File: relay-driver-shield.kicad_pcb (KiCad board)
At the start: 2 copper layers, 21 parts, among them J1 Screw_Terminal_01x02, J2 Screw_Terminal_01x02, J3 Screw_Terminal_01x02, J4 Screw_Terminal_01x02, Q1 2N7002, Q2 2N7002, Q3 2N7002, Q4 2N7002

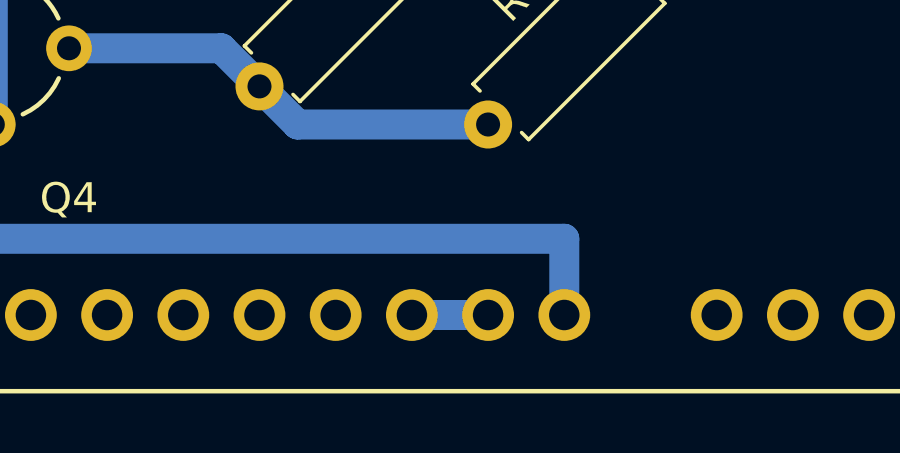
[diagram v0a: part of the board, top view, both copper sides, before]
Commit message: Removed bridge between GND1, GND2 and GND3 Not needed and avoids problems with Electrical Rule Checker
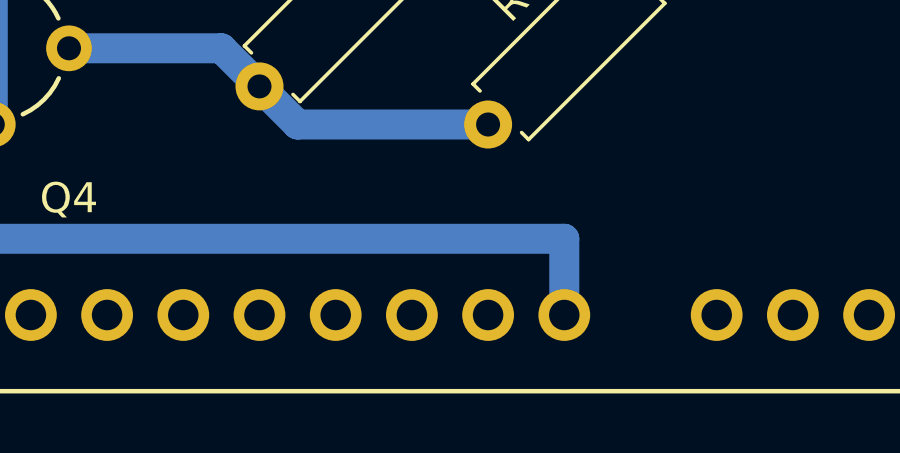
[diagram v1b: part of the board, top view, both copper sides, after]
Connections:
- ARD1 pad GND2: GND -> (no net)
- ARD1 pad GND3: GND -> (no net)
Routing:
- net GND: track 104.6 -> 102.0 mm
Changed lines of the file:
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@@
 (kicad_pcb (version 4) (host pcbnew 4.0.7)
   (general
-    (links 38)
-    (no_connects 1)
-    (area 102.594999 58.969 178.075001 114.75)
+    (links 36)
+    (no_connects 0)
+    (area 0 0 0 0)
     (thickness 1.6)
     (drawings 0)
-    (tracks 95)
+    (tracks 94)
     (zones 0)
     (modules 21)
@@
     (pad VIN thru_hole oval (at 45.72 -2.54) (size 1.7272 1.7272) (drill 1.016) (layers *.Cu *.Mask)
       (net 1 +12V))
-    (pad GND3 thru_hole oval (at 43.18 -2.54) (size 1.7272 1.7272) (drill 1.016) (layers *.Cu *.Mask)
-      (net 2 GND))
-    (pad GND2 thru_hole oval (at 40.64 -2.54) (size 1.7272 1.7272) (drill 1.016) (layers *.Cu *.Mask)
-      (net 2 GND))
+    (pad GND3 thru_hole oval (at 43.18 -2.54) (size 1.7272 1.7272) (drill 1.016) (layers *.Cu *.Mask))
+    (pad GND2 thru_hole oval (at 40.64 -2.54) (size 1.7272 1.7272) (drill 1.016) (layers *.Cu *.Mask))
     (pad 5V1 thru_hole oval (at 38.1 -2.54) (size 1.7272 1.7272) (drill 1.016) (layers *.Cu *.Mask))
     (pad 3.3V thru_hole oval (at 35.56 -2.54) (size 1.7272 1.7272) (drill 1.016) (layers *.Cu *.Mask))
@@
   (segment (start 129.54 100.33) (end 115.57 100.33) (width 1) (layer B.Cu) (net 1))
   (segment (start 129.54 90.17) (end 115.57 90.17) (width 1) (layer B.Cu) (net 1))
-  (segment (start 150.168154 68.271846) (end 135.636 68.271846) (width 1) (layer B.Cu) (net 2) (status 400000))
+  (segment (start 150.168154 68.271846) (end 135.636 68.271846) (width 1) (layer B.Cu) (net 2))
   (segment (start 135.89 68.58) (end 135.636 68.58) (width 1) (layer B.Cu) (net 2))
   (segment (start 135.89 68.525846) (end 135.89 68.58) (width 1) (layer B.Cu) (net 2))
   (segment (start 135.636 68.271846) (end 135.89 68.525846) (width 1) (layer B.Cu) (net 2))
-  (segment (start 150.168154 98.751846) (end 135.89 98.751846) (width 1) (layer B.Cu) (net 2) (status 400000))
+  (segment (start 150.168154 98.751846) (end 135.89 98.751846) (width 1) (layer B.Cu) (net 2))
   (segment (start 135.89 98.751846) (end 135.89 99.06) (width 1) (layer B.Cu) (net 2))
-  (segment (start 150.168154 88.591846) (end 135.89 88.591846) (width 1) (layer B.Cu) (net 2) (status 400000))
+  (segment (start 150.168154 88.591846) (end 135.89 88.591846) (width 1) (layer B.Cu) (net 2))
   (segment (start 135.89 88.591846) (end 135.89 88.9) (width 1) (layer B.Cu) (net 2))
-  (segment (start 150.168154 78.431846) (end 135.89 78.431846) (width 1) (layer B.Cu) (net 2) (status 400000))
+  (segment (start 150.168154 78.431846) (end 135.89 78.431846) (width 1) (layer B.Cu) (net 2))
   (segment (start 135.89 78.431846) (end 135.89 78.74) (width 1) (layer B.Cu) (net 2))
-  (segment (start 135.89 95.25) (end 135.89 99.06) (width 1) (layer B.Cu) (net 2) (status 400000))
-  (segment (start 135.89 99.06) (end 135.89 105.41) (width 1) (layer B.Cu) (net 2) (status 800000))
-  (segment (start 135.89 85.09) (end 135.89 88.9) (width 1) (layer B.Cu) (net 2) (status 400000))
-  (segment (start 135.89 88.9) (end 135.89 95.25) (width 1) (layer B.Cu) (net 2) (status 800000))
-  (segment (start 135.89 74.93) (end 135.89 78.74) (width 1) (layer B.Cu) (net 2) (status 400000))
-  (segment (start 135.89 78.74) (end 135.89 85.09) (width 1) (layer B.Cu) (net 2) (status 800000))
-  (segment (start 135.636 63.5) (end 135.636 68.58) (width 1) (layer B.Cu) (net 2) (status 400000))
-  (segment (start 135.636 68.58) (end 135.636 74.676) (width 1) (layer B.Cu) (net 2) (status 800000))
-  (segment (start 135.636 74.676) (end 135.89 74.93) (width 1) (layer B.Cu) (net 2) (status C00000))
-  (segment (start 149.86 111.76) (end 152.4 111.76) (width 1) (layer B.Cu) (net 2))
+  (segment (start 135.89 95.25) (end 135.89 99.06) (width 1) (layer B.Cu) (net 2))
+  (segment (start 135.89 99.06) (end 135.89 105.41) (width 1) (layer B.Cu) (net 2))
+  (segment (start 135.89 85.09) (end 135.89 88.9) (width 1) (layer B.Cu) (net 2))
+  (segment (start 135.89 88.9) (end 135.89 95.25) (width 1) (layer B.Cu) (net 2))
+  (segment (start 135.89 74.93) (end 135.89 78.74) (width 1) (layer B.Cu) (net 2))
+  (segment (start 135.89 78.74) (end 135.89 85.09) (width 1) (layer B.Cu) (net 2))
+  (segment (start 135.636 63.5) (end 135.636 68.58) (width 1) (layer B.Cu) (net 2))
+  (segment (start 135.636 68.58) (end 135.636 74.676) (width 1) (layer B.Cu) (net 2))
+  (segment (start 135.636 74.676) (end 135.89 74.93) (width 1) (layer B.Cu) (net 2))
   (segment (start 150.476308 78.74) (end 150.168154 78.431846) (width 0.25) (layer B.Cu) (net 2) (status 30))
   (segment (start 150.168154 68.271846) (end 149.551846 68.271846) (width 0.25) (layer B.Cu) (net 2) (status 30))

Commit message: Added values to the resistors and diodes
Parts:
- D1, D2, D3, D4: value D -> 1N4004
- R1, R3, R5, R7: value R -> 1K
- R2, R4, R6, R8: value R -> 10K
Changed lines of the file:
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@@
       (effects (font (size 1 1) (thickness 0.15)))
     )
-    (fp_text value D (at 3.81 2.41 225) (layer F.Fab)
+    (fp_text value 1N4004 (at 3.81 2.41 225) (layer F.Fab)
       (effects (font (size 1 1) (thickness 0.15)))
     )
@@
       (effects (font (size 1 1) (thickness 0.15)))
     )
-    (fp_text value D (at 3.81 2.41 225) (layer F.Fab)
+    (fp_text value 1N4004 (at 3.81 2.41 225) (layer F.Fab)
       (effects (font (size 1 1) (thickness 0.15)))
     )
@@
       (effects (font (size 1 1) (thickness 0.15)))
     )
-    (fp_text value D (at 3.81 2.41 225) (layer F.Fab)
+    (fp_text value 1N4004 (at 3.81 2.41 225) (layer F.Fab)
       (effects (font (size 1 1) (thickness 0.15)))
     )
@@
       (effects (font (size 1 1) (thickness 0.15)))
     )
-    (fp_text value D (at 3.81 2.41 225) (layer F.Fab)
+    (fp_text value 1N4004 (at 3.81 2.41 225) (layer F.Fab)
       (effects (font (size 1 1) (thickness 0.15)))
     )
@@
       (effects (font (size 1 1) (thickness 0.15)))
     )
-    (fp_text value R (at 3.81 2.31 45) (layer F.Fab)
+    (fp_text value 1K (at 3.81 2.31 45) (layer F.Fab)
       (effects (font (size 1 1) (thickness 0.15)))
     )
@@
       (effects (font (size 1 1) (thickness 0.15)))
     )
-    (fp_text value R (at 3.81 2.31 45) (layer F.Fab)
+    (fp_text value 10K (at 3.81 2.31 45) (layer F.Fab)
       (effects (font (size 1 1) (thickness 0.15)))
     )
@@
       (effects (font (size 1 1) (thickness 0.15)))
     )
-    (fp_text value R (at 3.81 2.31 45) (layer F.Fab)
+    (fp_text value 1K (at 3.81 2.31 45) (layer F.Fab)
       (effects (font (size 1 1) (thickness 0.15)))
     )
@@
       (effects (font (size 1 1) (thickness 0.15)))
     )
-    (fp_text value R (at 3.81 2.31 45) (layer F.Fab)
+    (fp_text value 10K (at 3.81 2.31 45) (layer F.Fab)
       (effects (font (size 1 1) (thickness 0.15)))
     )
@@
       (effects (font (size 1 1) (thickness 0.15)))
     )
-    (fp_text value R (at 3.81 2.31 45) (layer F.Fab)
+    (fp_text value 1K (at 3.81 2.31 45) (layer F.Fab)
       (effects (font (size 1 1) (thickness 0.15)))
     )
@@
       (effects (font (size 1 1) (thickness 0.15)))
     )
-    (fp_text value R (at 3.81 2.31 45) (layer F.Fab)
+    (fp_text value 10K (at 3.81 2.31 45) (layer F.Fab)
       (effects (font (size 1 1) (thickness 0.15)))
     )
@@
       (effects (font (size 1 1) (thickness 0.15)))
     )
-    (fp_text value R (at 3.81 2.31 45) (layer F.Fab)
+    (fp_text value 1K (at 3.81 2.31 45) (layer F.Fab)
       (effects (font (size 1 1) (thickness 0.15)))
     )
@@
       (effects (font (size 1 1) (thickness 0.15)))
     )
-    (fp_text value R (at 3.81 2.31 45) (layer F.Fab)
-      (effects (font (size 1 1) (thickness 0.15)))
-    )
+    (fp_text value 10K (at 3.81 2.31 45) (layer F.Fab)
+      (effects (font (size 1 1) (thickness 0.15)))
+    )

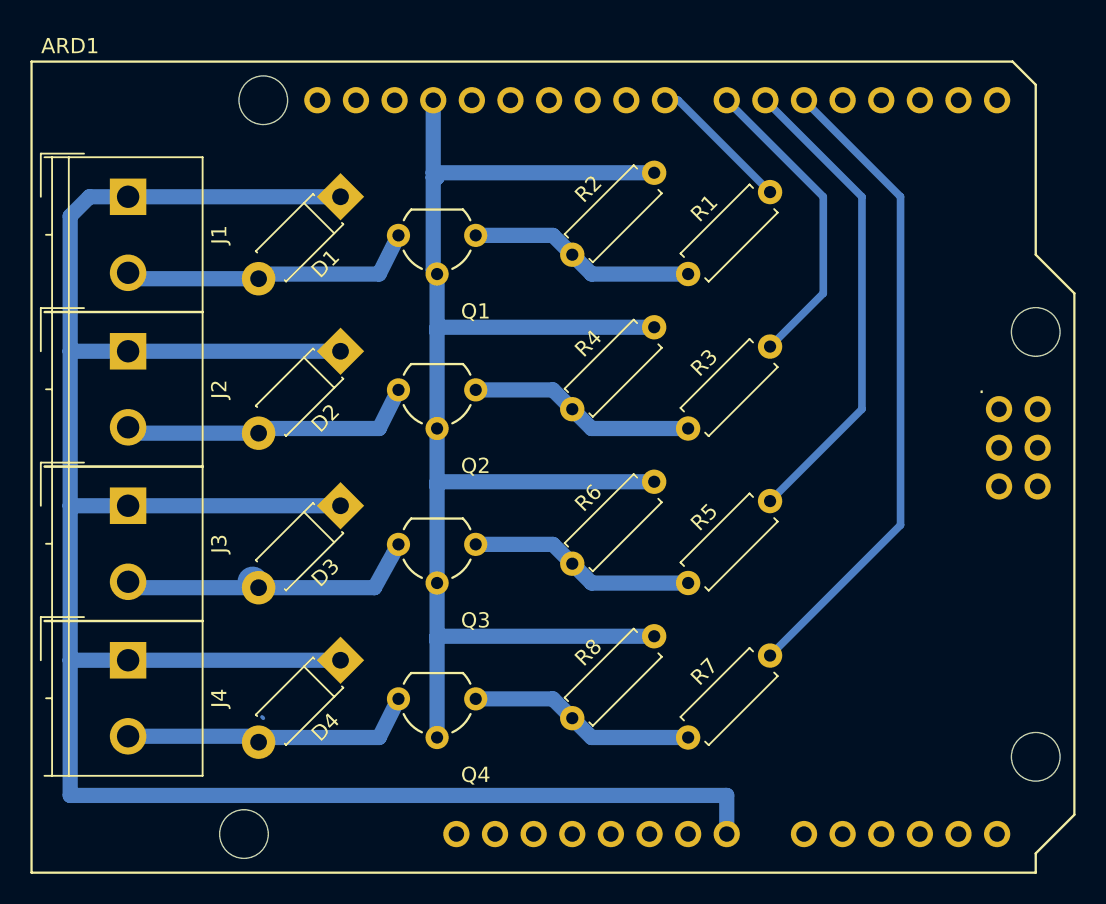
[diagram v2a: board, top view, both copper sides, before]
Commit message: Moved components closer together on PCB
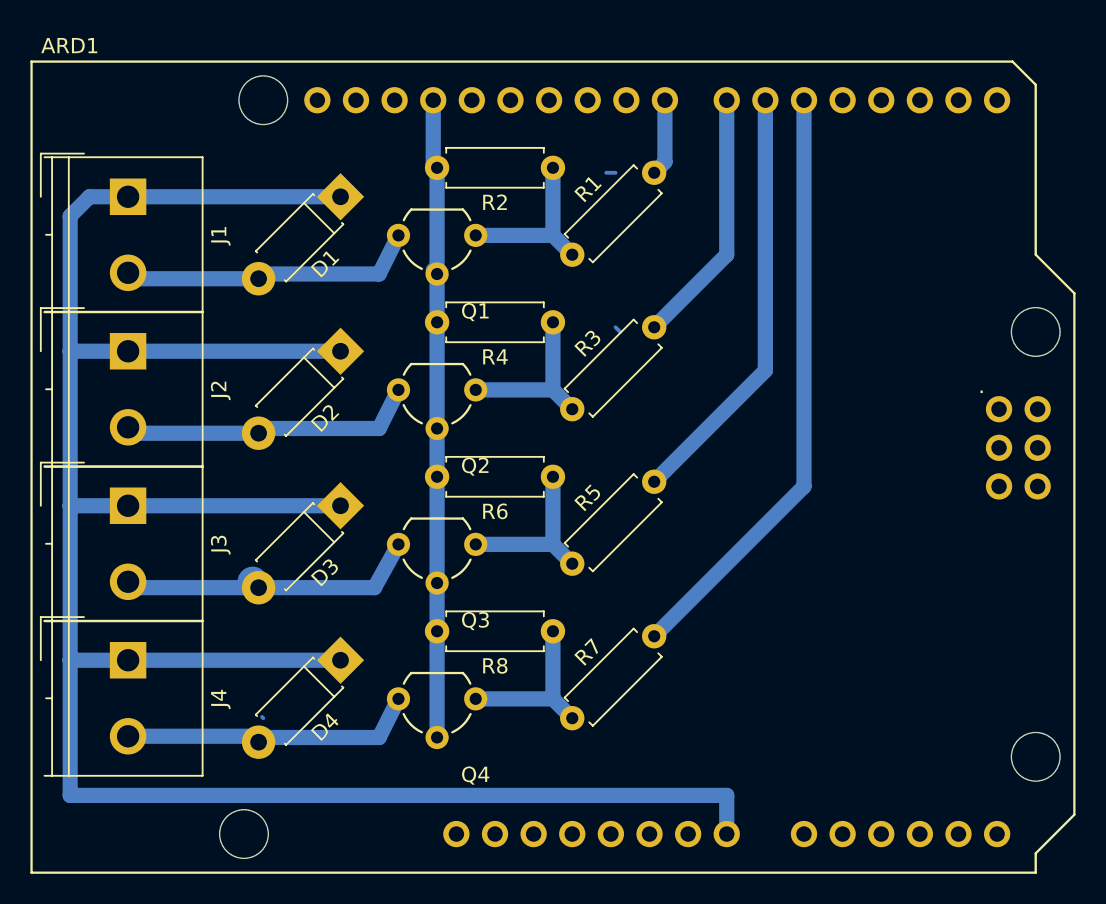
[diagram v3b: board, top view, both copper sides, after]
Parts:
- moved R1 7.73 mm to (144.8, 73.7)
- moved R3 7.73 mm to (144.8, 83.8)
- moved R5 7.73 mm to (144.8, 94.0)
- moved R7 7.73 mm to (144.8, 104.1)
- moved R2 5.85 mm to (143.5, 67.9), turned to 180 degrees
- moved R6 5.85 mm to (143.5, 88.3), turned to 180 degrees
- moved R8 5.85 mm to (143.5, 98.4), turned to 180 degrees
- moved R4 5.85 mm to (143.5, 78.1), turned to 180 degrees
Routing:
- net GND: track 102.0 -> 42.7 mm
- net Net-(ARD1-PadD8): track 9.67 -> 5.32 mm
- net Net-(Q2-Pad1): track 15.0 -> 11.3 mm
- net Net-(Q3-Pad1): track 15.0 -> 11.3 mm
- net Net-(Q1-Pad1): track 15.0 -> 11.3 mm
- net Net-(Q4-Pad1): track 15.0 -> 11.3 mm
- net Net-(ARD1-PadD6): track 31.5 -> 28.1 mm
- net Net-(ARD1-PadD7): track 20.3 -> 16.9 mm
- net Net-(ARD1-PadD5): track 42.7 -> 39.3 mm
- net (no net): track 0.11 -> 1.17 mm
